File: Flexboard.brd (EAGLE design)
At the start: 488.2 x 145.3 mm, 421 parts, among them U1 MK22FX512AVLQ12

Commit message: Added usb to MCU and routed power planes
Added board wide power and ground planes, as well as USB traces to kinetis MCU.

Signed-off-by: Daniel DeGrasse <daniel@degrasse.com>
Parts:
- added J1: USB4105-GF-A, USB4105-GF-A:GCT_USB4105-GF-A
- moved SJ_MCU_LED_ROW1 9.98 mm to (344.4, 110.7)
- moved SJ_MCU_ROW2 7.22 mm to (332.4, 110.7)
- moved SJ_MCU_ROW1 6.61 mm to (329.6, 118.9)
- moved SJ_MCU_LED_ROW2 6.59 mm to (329.6, 110.7)
- moved SJ_R1 6.06 mm to (329.7, 123.8)
- moved SJ_LED_R1 5.80 mm to (346.3, 123.8)
- moved D17 4.76 mm to (328.6, 142.9)
- moved D37 3.70 mm to (329.7, 119.0)
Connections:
- removed net VOUT33: U1.21
- removed net VREGIN: U1.22
- new net USB_N: J1.A7, J1.B7, U1.20
- new net USB_P: J1.A6, J1.B6, U1.19
- new net VBUS: J1.A4_B9, J1.B4_A9, U1.22
- net GND: now also J1.A1_B12, J1.B1_A12, J1.S1, J1.S2, J1.S3, J1.S4
- net VDD_3V3: now also U1.21
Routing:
- net VDD_3V3: track 0.00 -> 80.5 mm
- net LED_ROW_2{SB}: track 370.2 -> 331.6 mm, vias 1 -> 0
- net GND: track 0.00 -> 26.6 mm, vias 0 -> 10
- net ROW_2{SB}: track 370.4 -> 347.9 mm, vias 5 -> 4
- net ROW_1: track 397.0 -> 376.3 mm, vias 1 -> 0
- net VBUS: track 0.00 -> 19.5 mm, vias 0 -> 1
- net LED_ROW_1{MCU}: track 17.2 -> 0.00 mm, vias 1 -> 0
- net ROW_1{MCU}: track 15.3 -> 0.00 mm, vias 1 -> 0
- net USB_P: track 0.00 -> 12.9 mm, vias 0 -> 1
- net USB_N: track 0.00 -> 12.9 mm, vias 0 -> 1
- net ROW_2{MCU}: track 11.5 -> 0.00 mm, vias 1 -> 0
- net LED_ROW_2{MCU}: track 9.48 -> 0.00 mm, vias 1 -> 0
- net N$34: track 8.18 -> 4.52 mm
- net LED_ROW_1: track 403.1 -> 399.8 mm, vias 1 -> 0
- net N$33: track 7.77 -> 4.93 mm
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- added copper zone on layer 1, net GND
- added copper zone on layer 16, net GND

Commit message: Routed diodes around usb
All required diodes and solder bridges for keys are now routed to MCU

Signed-off-by: Daniel DeGrasse <daniel@degrasse.com>
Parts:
- moved SJ_MCU_LED_ROW1 7.11 mm to (344.8, 117.8)
- moved SJ_MCU_ROW2 1.04 mm to (332.7, 111.7)
- moved SJ_MCU_LED_ROW2 0.21 mm to (329.6, 110.5), flipped to the bottom
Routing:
- net LED_ROW_2{SB}: track 331.6 -> 363.9 mm
- net ROW_2{SB}: track 347.9 -> 372.8 mm, vias 4 -> 5
- net LED_ROW_1{MCU}: track 0.00 -> 20.8 mm, vias 0 -> 3
- net ROW_1: track 376.3 -> 395.8 mm, vias 0 -> 1
- net ROW_1{MCU}: track 0.00 -> 11.8 mm, vias 0 -> 1
- net ROW_2{MCU}: track 0.00 -> 4.80 mm, vias 0 -> 1
- net LED_ROW_1{SB}: track 0.26 -> 4.89 mm
- net LED_ROW_1: track 399.8 -> 403.1 mm, vias 0 -> 1
- net ROW_1{SB}: track 0.00 -> 3.13 mm
- net LED_ROW_2{MCU}: track 0.00 -> 2.47 mm

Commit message: Added decoupling capacitors around the mcu
added power caps to MCU, 1uF and 100nF

Signed-off-by: Daniel DeGrasse <daniel@degrasse.com>
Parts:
- added C1: 1000pF, C1206C102K1RACAUTO:CAPC3216X110N
- added C2, C3, C4, C8: 1uF, GCM31MR71H105KA55L:CAPC3216X125N
- added C5, C6, C7, C9: 100nF, C1206C104K5RAC7800:CAPC3216X88N
- added R1: 10k, CRGCQ1206J10K:RESC3115X65N
- added SW1: 1825910-7, 1825910-7:SW_1825910-7
- added U$1: GRPB052VWQS-RC, GRPB052VWQS-RC:DEBUG
- moved D2 6.74 mm to (35.7, 138.1)
- moved D13 5.32 mm to (254.8, 138.1)
- moved D14 5.32 mm to (273.8, 138.1)
- moved D19 5.32 mm to (378.6, 138.1)
- moved D8 5.32 mm to (159.5, 138.1)
- moved D5 5.32 mm to (102.4, 138.1)
- moved D6 5.32 mm to (121.4, 138.1)
- moved D1 5.32 mm to (16.7, 138.1)
- moved D10 5.32 mm to (197.6, 138.1)
- moved D11 5.32 mm to (216.7, 138.1)
- moved D12 5.32 mm to (235.7, 138.1)
- moved D3 5.32 mm to (64.3, 138.1)
- moved D4 5.32 mm to (83.3, 138.1)
- moved D7 5.32 mm to (140.5, 138.1)
- moved D9 5.32 mm to (178.6, 138.1)
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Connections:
- removed net JTAG_TRST: U1.55
- removed net VBAT: U1.42
- removed net VDDA: U1.31
- removed net VREFH: U1.32
- removed net VREFL: U1.33
- removed net VSSA: U1.34
- new net EXTAL: U1.72
- new net EXTAL32: U1.41
- new net NMI: U1.54
- new net XTAL: U1.73
- new net XTAL32: U1.40
- net COL_18{MCU}: now also U1.66; no longer U1.65
- net COL_19{MCU}: now also U1.64; no longer U1.63
- net COL_20{MCU}: now also U1.62; no longer U1.61
- net COL_21{MCU}: now also U1.60; no longer U1.59
- net COL_22{MCU}: now also U1.58; no longer U1.54
- net GND: now also C1.2, C2.2, C3.2, C4.2, C5.1, C6.1, C7.1, C8.2, C9.1, SW1.3, SW1.4, U$1.3, U$1.5, U1.33, U1.34
- net JTAG_TCLK/SWD_CLK: now also U$1.4
- net JTAG_TDI: now also U$1.8
- net JTAG_TDO/TRACE_SWO: now also U$1.6
- net JTAG_TMS/SWD_DIO: now also U$1.2
- net LED_COL_18{MCU}: now also U1.65; no longer U1.64
- net LED_COL_19{MCU}: now also U1.63; no longer U1.62
- net LED_COL_20{MCU}: now also U1.61; no longer U1.60
- net LED_COL_21{MCU}: now also U1.59; no longer U1.58
- net RESET: now also C1.1, R1.1, SW1.1, SW1.2, U$1.10
- net VDD_3V3: now also C2.1, C3.1, C4.1, C5.2, C6.2, C7.2, C8.1, C9.2, R1.2, U$1.1, U1.31, U1.32, U1.42
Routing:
- net RESET: track 0.00 -> 67.9 mm, vias 0 -> 3
- net VDD_3V3: track 80.5 -> 139.0 mm, vias 0 -> 7
- net GND: track 26.6 -> 78.4 mm, vias 10 -> 13
- net JTAG_TDI: track 0.00 -> 26.4 mm, vias 0 -> 1
- net JTAG_TDO/TRACE_SWO: track 0.00 -> 25.7 mm, vias 0 -> 1
- net JTAG_TCLK/SWD_CLK: track 0.00 -> 24.1 mm, vias 0 -> 1
- net ROW_1: track 395.8 -> 419.4 mm
- net JTAG_TMS/SWD_DIO: track 0.00 -> 22.1 mm, vias 0 -> 1
- net LED_COL_7: track 101.0 -> 120.8 mm
- net COL_7: track 97.9 -> 105.2 mm
- net N$35: track 7.87 -> 3.68 mm
- net N$37: track 7.77 -> 3.68 mm
- net N$27: track 7.77 -> 3.68 mm
- net N$25: track 7.77 -> 3.68 mm
- net N$15: track 7.77 -> 3.68 mm
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
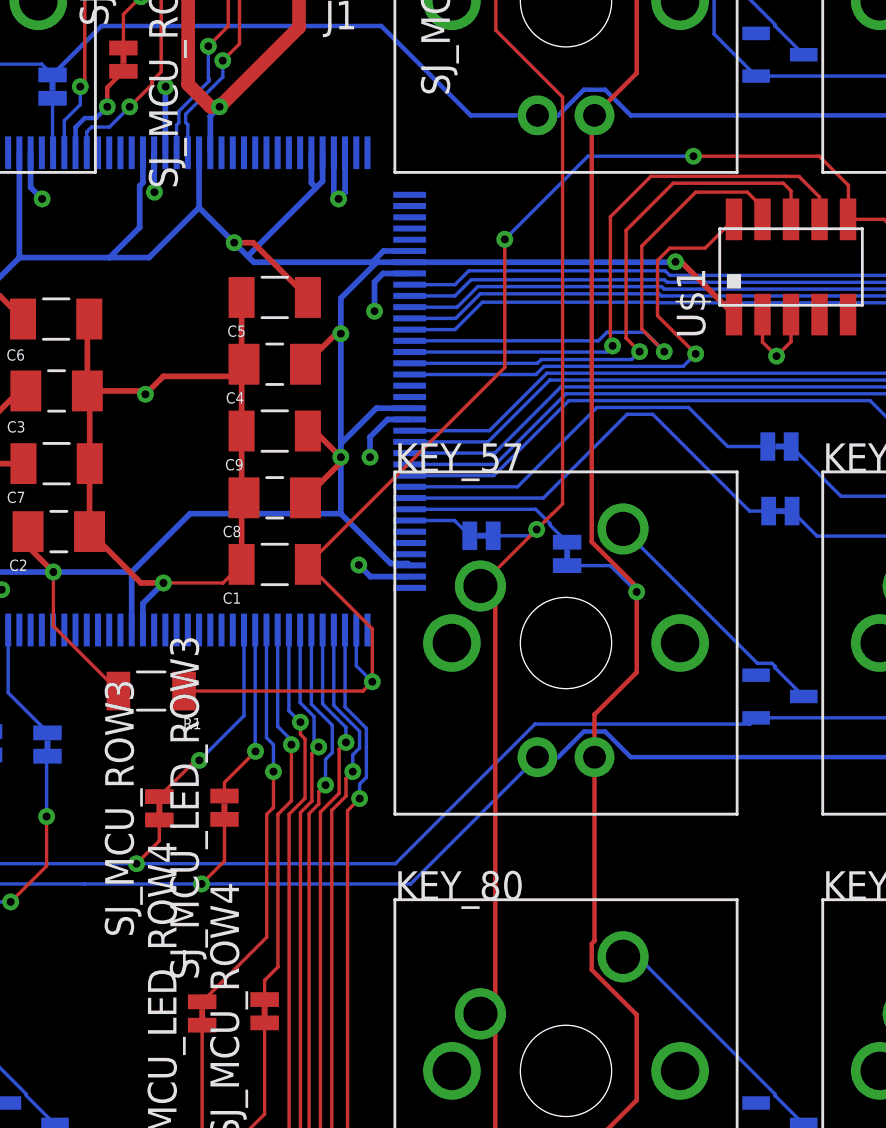
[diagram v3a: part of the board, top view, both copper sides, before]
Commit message: added oscillators to design
added 8MHz and 32KHz crystals to design. Still need to add capacitors
and resistors for USB 5V as well as DP/DN

Signed-off-by: Daniel DeGrasse <daniel@degrasse.com>
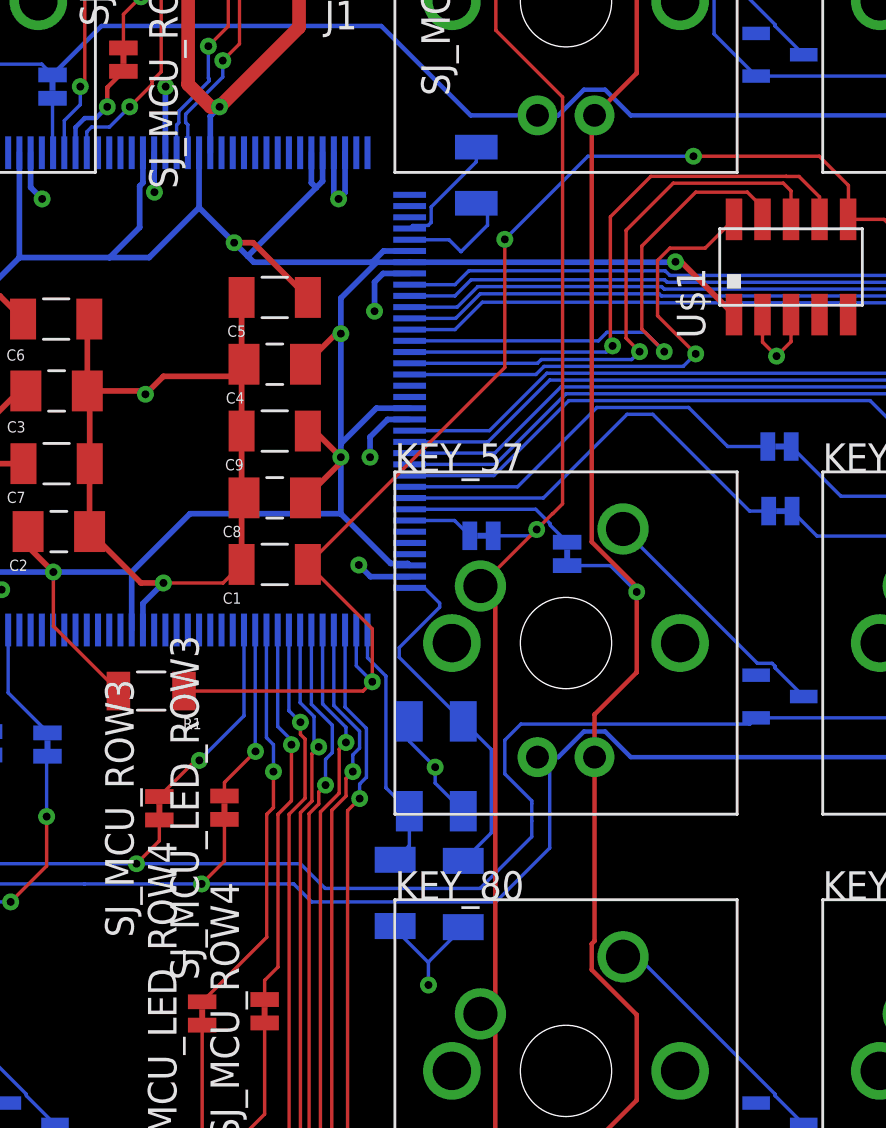
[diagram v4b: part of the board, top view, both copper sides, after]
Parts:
- added C10, C11: 22pF, C1206C220JGGAC7800:CAPC3216X110N
- added Y1: ABM3B-8.000MHZ-B2-T, ABM3B-8.000MHZ-B2-T:OSC_ABM3B-8.000MHZ-B2-T
- added Y2: ABS07-32.768KHZ-T, ABS07-32.768KHZ-T:XTAL_ABS07-32.768KHZ-T
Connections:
- net EXTAL: now also C11.2, Y1.3
- net EXTAL32: now also Y2.1
- net GND: now also C10.1, C11.1, Y1.2, Y1.4
- net XTAL: now also C10.2, Y1.1
- net XTAL32: now also Y2.2
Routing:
- net EXTAL: track 0.00 -> 16.1 mm
- net XTAL: track 0.00 -> 11.3 mm
- net GND: track 78.4 -> 88.8 mm, vias 13 -> 15
- net EXTAL32: track 0.00 -> 5.36 mm
- net XTAL32: track 0.00 -> 5.26 mm
- net ROW_3{SB}: track 380.5 -> 385.6 mm
- net LED_ROW_3{SB}: track 381.6 -> 385.3 mm

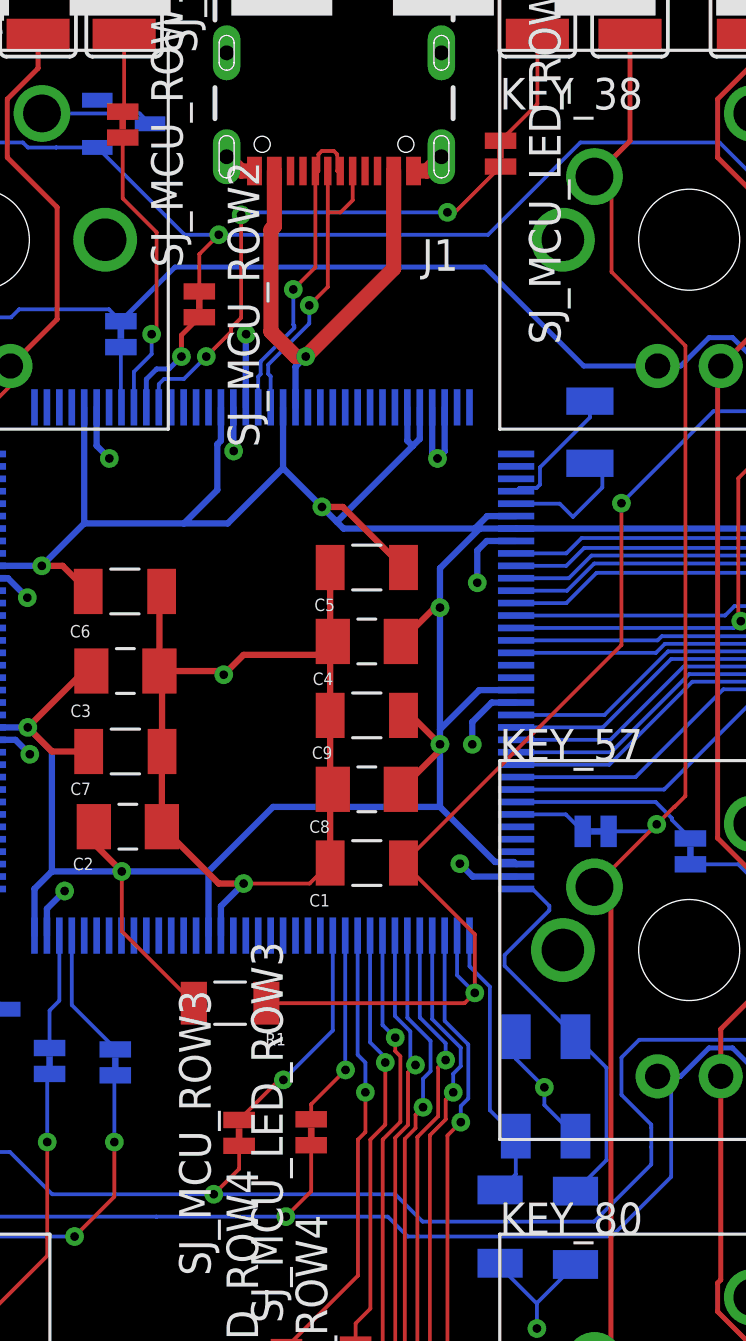
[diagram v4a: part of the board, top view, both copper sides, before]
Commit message: added usb 33 ohm resistors
Added 33 ohm resistors to usb traces, and redid length matching

Signed-off-by: Daniel DeGrasse <daniel@degrasse.com>
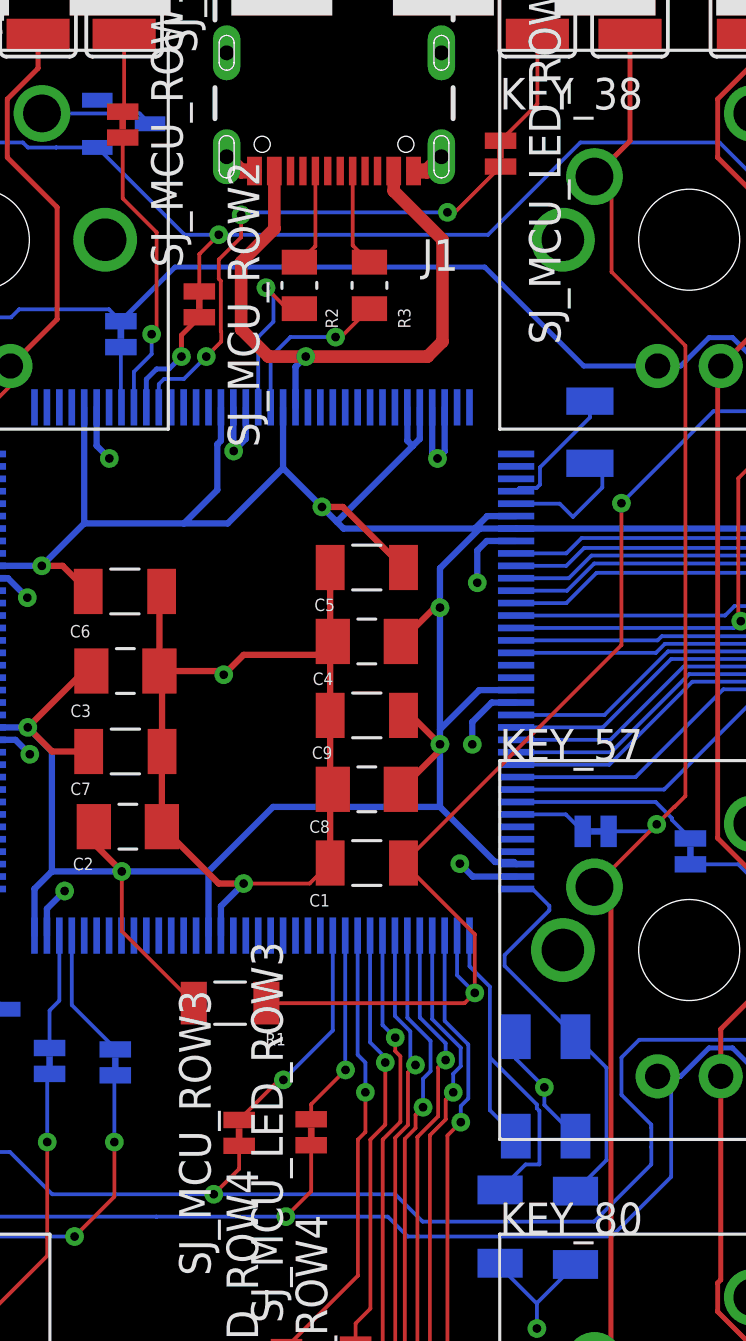
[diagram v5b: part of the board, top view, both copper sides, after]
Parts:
- added R2, R3: 33, CRG0805F33R:RESC2012X65N
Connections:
- new net USB_MCU_N: R3.2, U1.20
- new net USB_MCU_P: R2.2, U1.19
- net USB_N: now also R3.1; no longer U1.20
- net USB_P: now also R2.1; no longer U1.19
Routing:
- net USB_P: track 12.9 -> 3.93 mm, vias 1 -> 0
- net USB_N: track 12.9 -> 3.95 mm, vias 1 -> 0
- net USB_MCU_P: track 0.00 -> 6.88 mm, vias 0 -> 1
- net USB_MCU_N: track 0.00 -> 6.81 mm, vias 0 -> 1
- net VBUS: track 19.5 -> 25.6 mm
- net XTAL: track 11.3 -> 16.1 mm
- net GND: track 88.8 -> 87.8 mm, vias 15 -> 14

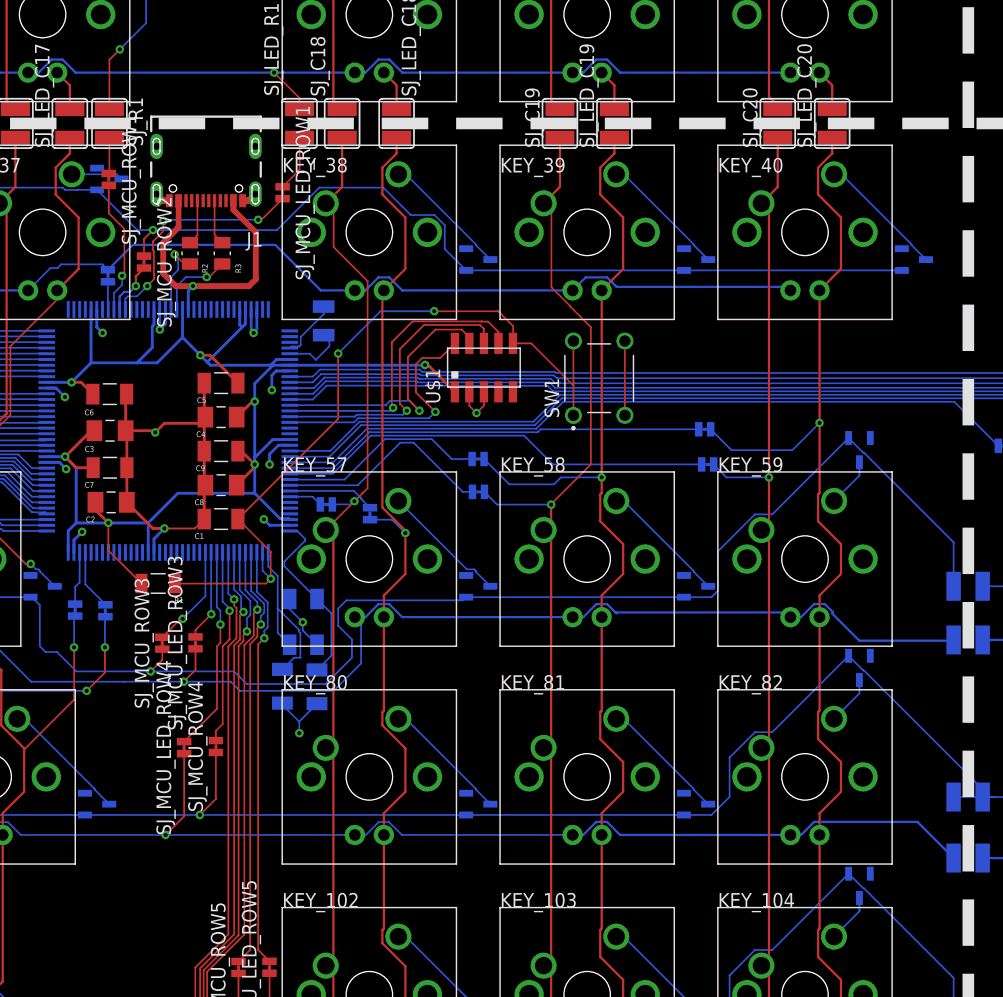
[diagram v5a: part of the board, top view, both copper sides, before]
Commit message: added TVS diodes for ESD protection and power source switch
TVS diodes required for high voltage spike protection, power
source switch will enable selection of LDO or internal regulator

Signed-off-by: Daniel DeGrasse <daniel@degrasse.com>
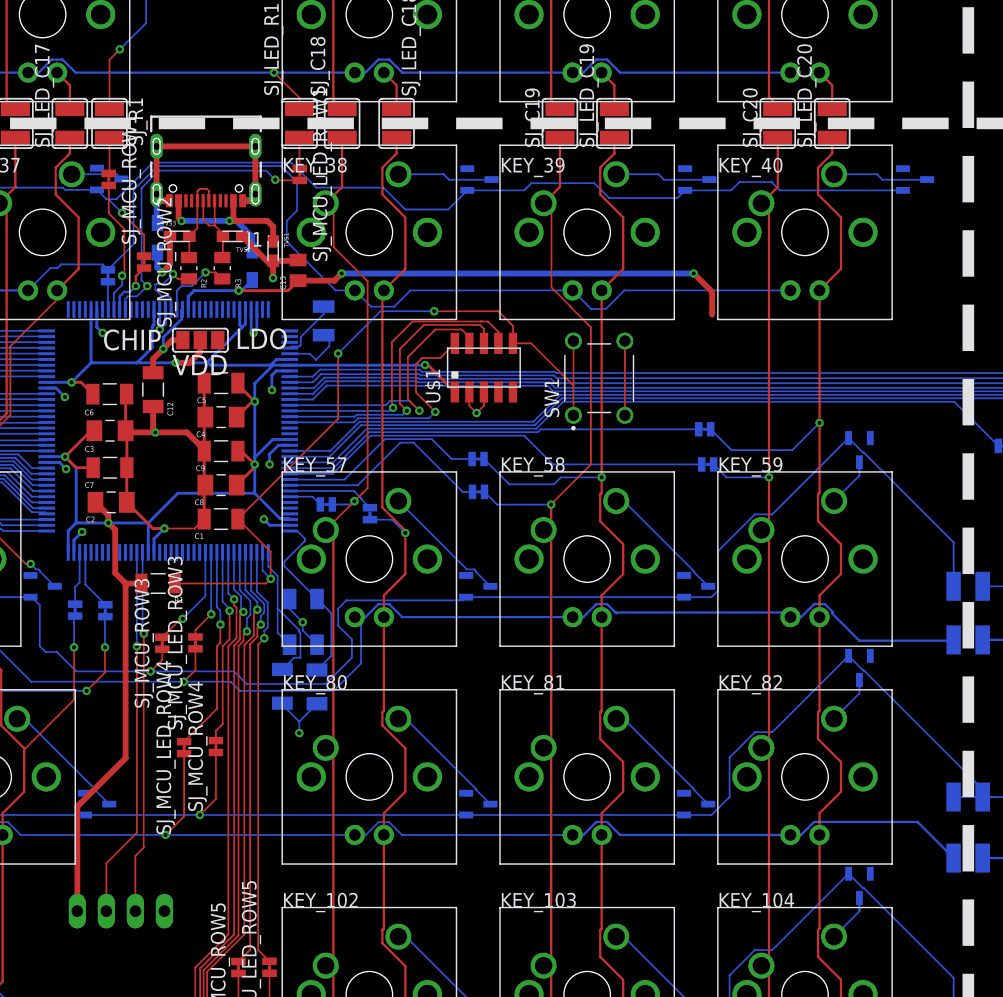
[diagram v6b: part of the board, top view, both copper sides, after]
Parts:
- added C12: 2.2uF, 1206ZC225MAT2A:CAPC3216X178N
- added C13: 10uF, GRM21BC8YA106ME11L:CAPC2012X145N
- added L1, L2: 330, 782853331:78285333
- added SJ1: (no value), jumper:SJ_2
- added SV1: (no value), con-lstb:MA04-1
- added TVS1, TVS2, TVS3: (no value), 0603ESDA2-TR2:0603ESDA2-TR2
- moved D38 7.00 mm to (362.1, 118.9)
- moved D39 7.00 mm to (381.1, 118.9)
- moved D40 7.00 mm to (400.1, 118.9)
- moved SJ_MCU_LED_ROW1 2.19 mm to (346.3, 119.4)
- moved R2 1.30 mm to (336.6, 111.2)
- moved R3 1.30 mm to (339.6, 111.2)
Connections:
- new net N$1: J1.S1, J1.S2, J1.S3, J1.S4, L2.1
- new net UART0_RX: SV1.3, U1.95
- new net UART0_TX: SV1.2, U1.96
- new net VLDO_33: SJ1.1
- new net VOUT_33: C12.1, SJ1.3, U1.21
- new net VSYS_5V5: C13.1, L1.2, U1.22
- net GND: now also C12.2, C13.2, L2.2, SV1.4, TVS1.2, TVS2.1, TVS3.1; no longer J1.S1, J1.S2, J1.S3, J1.S4
- net USB_N: now also TVS2.2
- net USB_P: now also TVS3.2
- net VBUS: now also L1.1, TVS1.1; no longer U1.22
- net VDD_3V3: now also SJ1.2, SV1.1; no longer U1.21
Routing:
- net VSYS_5V5: track 0.00 -> 52.0 mm, vias 0 -> 3
- net UART0_TX: track 0.00 -> 32.5 mm, vias 0 -> 1
- net UART0_RX: track 0.00 -> 31.7 mm, vias 0 -> 1
- net VDD_3V3: track 139.0 -> 168.1 mm
- net N$1: track 0.00 -> 19.5 mm
- net GND: track 87.8 -> 101.8 mm, vias 14 -> 16
- net LED_ROW_2{SB}: track 363.9 -> 377.3 mm
- net VOUT_33: track 0.00 -> 8.64 mm, vias 0 -> 1
- net VBUS: track 25.6 -> 17.0 mm, vias 1 -> 2
- net LED_ROW_1{MCU}: track 20.9 -> 26.9 mm, vias 3 -> 2
- net USB_N: track 3.95 -> 8.16 mm
- net USB_P: track 3.93 -> 8.11 mm
- net N$22: track 11.2 -> 8.35 mm
- net N$28: track 11.2 -> 8.35 mm
- net N$24: track 11.2 -> 8.35 mm
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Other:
- board text added: "3V3"
- board text added: "CHIP"
- board text added: "GND"
- board text added: "LDO"
- board text added: "UART_RX"
- board text added: "UART_TX"
- board text added: "VDD"
